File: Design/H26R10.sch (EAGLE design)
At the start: 39 parts, among them P1 HEXABIT_17.32_NO_P3_P6_P7_P12, P2 CON-PHOENIX-350_1751277, P3 1751251, U1 STM32F091CBU6, U2 AD8295BCPZ-WP, U3 AD8275BRMZ, U4 AD7687BRMZ, U5 ADR431ARMZ, X1 XTALL_CSTCE8M00G52

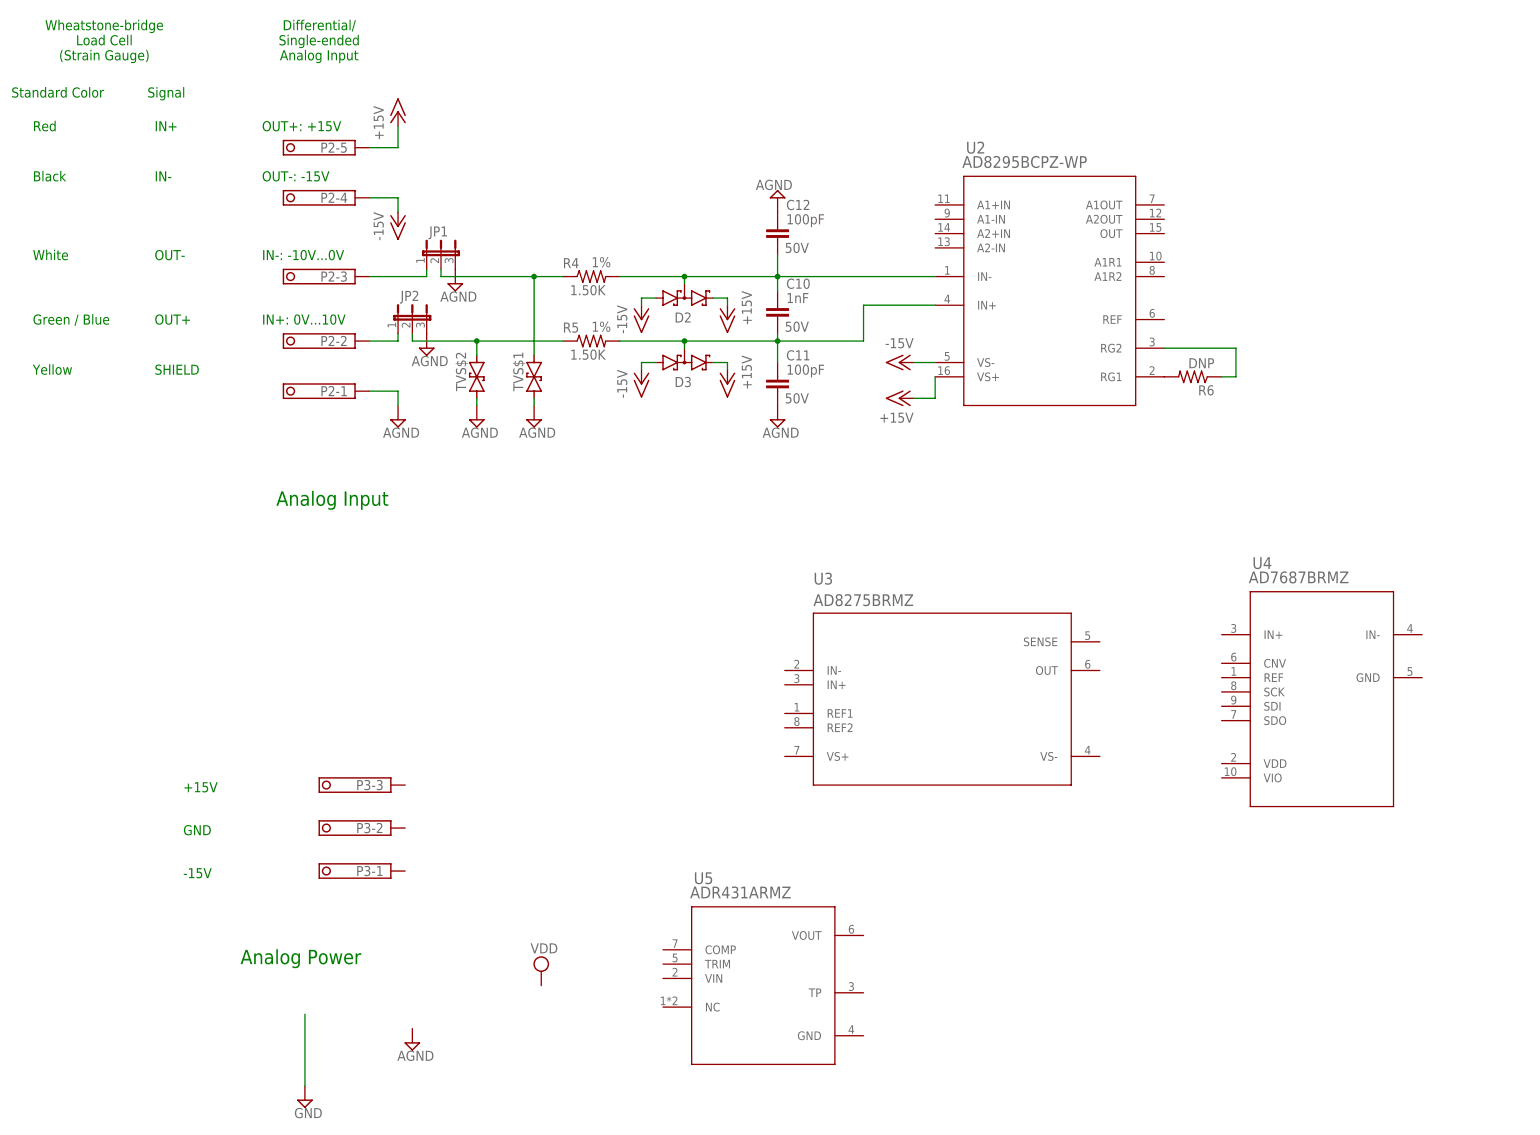
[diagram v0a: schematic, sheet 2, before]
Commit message: Finished analog power chain and some AD8295 connections
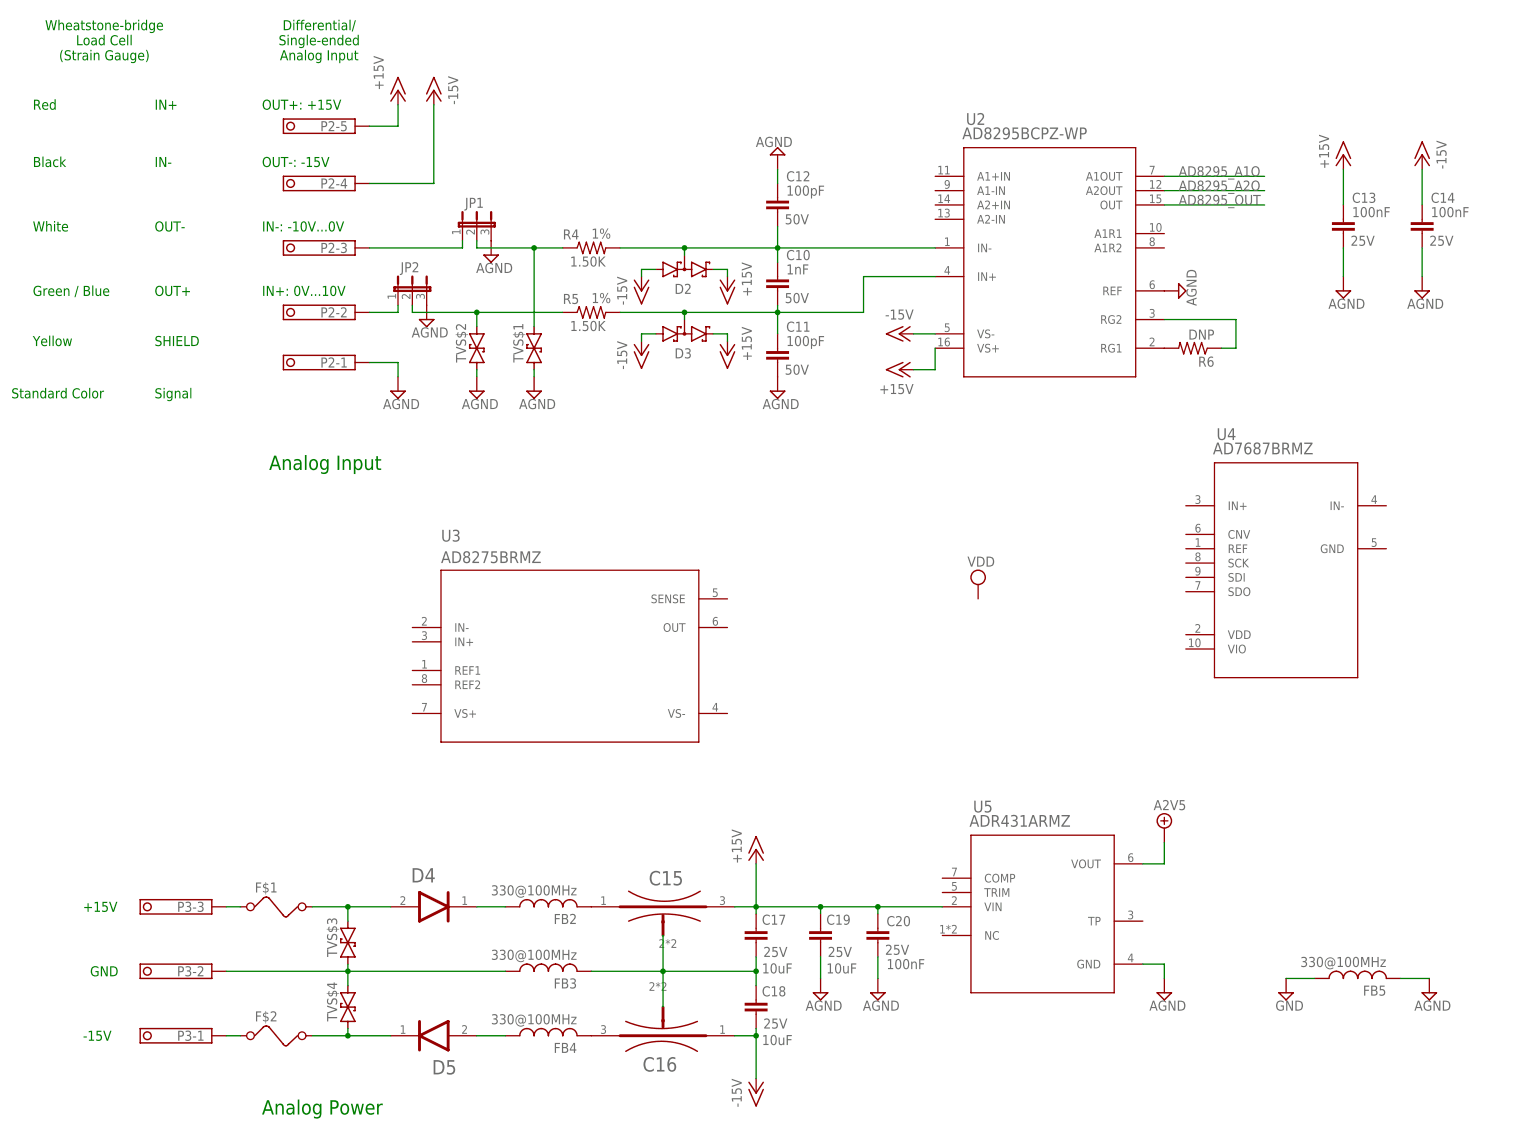
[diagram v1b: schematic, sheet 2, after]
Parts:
- removed FB1: FB-TDK_MMZ1608Y300B, Hexabitz:FB-TDK_MMZ1608Y300B
- added C13, C14, C20: 100nF, Hexabitz:C-0603
- added C15, C16: MURATA_NFM21PC105B1A3DMURATA_NFM21PC105B1A3D_0_0, Hexabitz:MURATA_NFM21PC105B1A3DMURATA_NFM21PC105B1A3D_0_0
- added C17, C18, C19: 10uF, Hexabitz:C-1206
- added D4, D5: DIODES_SBR2U30P1-7DIODES_SBR2U30P1-7_0_0, Hexabitz:DIODES_SBR2U30P1-7DIODES_SBR2U30P1-7_0_0
- added F$1, F$2: NANOSMDC035F-2120, Hexabitz:NANOSMDC035F-2120
- added FB2, FB3, FB4, FB5: 330@100MHz, Hexabitz:FB-0805
- added TVS$3, TVS$4: SMBJ30CA, Hexabitz:SMBJ30CA
- JP1, JP2: MFN (none) -> TE Connectivity; MPN (none) -> 5-146274-3; OCTOPART_URL (none) -> https://octopart.com/5-146274-3-te+connectivity-41331935?r=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
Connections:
- removed net VDDA: C1.1, C2.+, FB1.1, U1.VDDA
- new net +5V: U5.VOUT
- new net AD8295_A1O: U2.A1OUT
- new net AD8295_A2O: U2.A2OUT
- new net AD8295_OUT: U2.OUT
- new net N$15: F$1.1, P3-3.K
- new net N$16: F$2.1, P3-1.K
- new net N$17: D4.ANODE, F$1.2, TVS$3.2
- new net N$18: D5.CATHODE, F$2.2, TVS$4.1
- new net N$19: FB3.1, P3-2.K, TVS$3.1, TVS$4.2
- new net N$20: D4.CATHODE, FB2.1
- new net N$21: D5.ANODE, FB4.1
- new net N$22: C15.INPUT, FB2.2
- new net N$23: C16.OUTPUT, FB4.2
- new net N$24: C17.2, C18.1, FB3.2
- net +15V: now also C13.1, C15.OUTPUT, C17.1, C19.1, C20.1, U5.VIN
- net -15V: now also C14.1, C16.INPUT, C18.2
- net AGND: now also C13.2, C14.2, C19.2, C20.2, FB5.2, U2.REF, U5.GND
- net GND: now also C1.2, C2.-, FB5.1, U1.VSS_A
- net VDD: now also C1.1, C2.+, U1.VDDA; no longer FB1.2
- net VSSA: no longer C1.2, C2.-, U1.VSS_A
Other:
- moved on the sheet: C10, C11, C12, D2, D3, JP1, JP2, P2-1, P2-2, P2-3, P2-4, P2-5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

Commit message: Finished schematics. No ERC yet
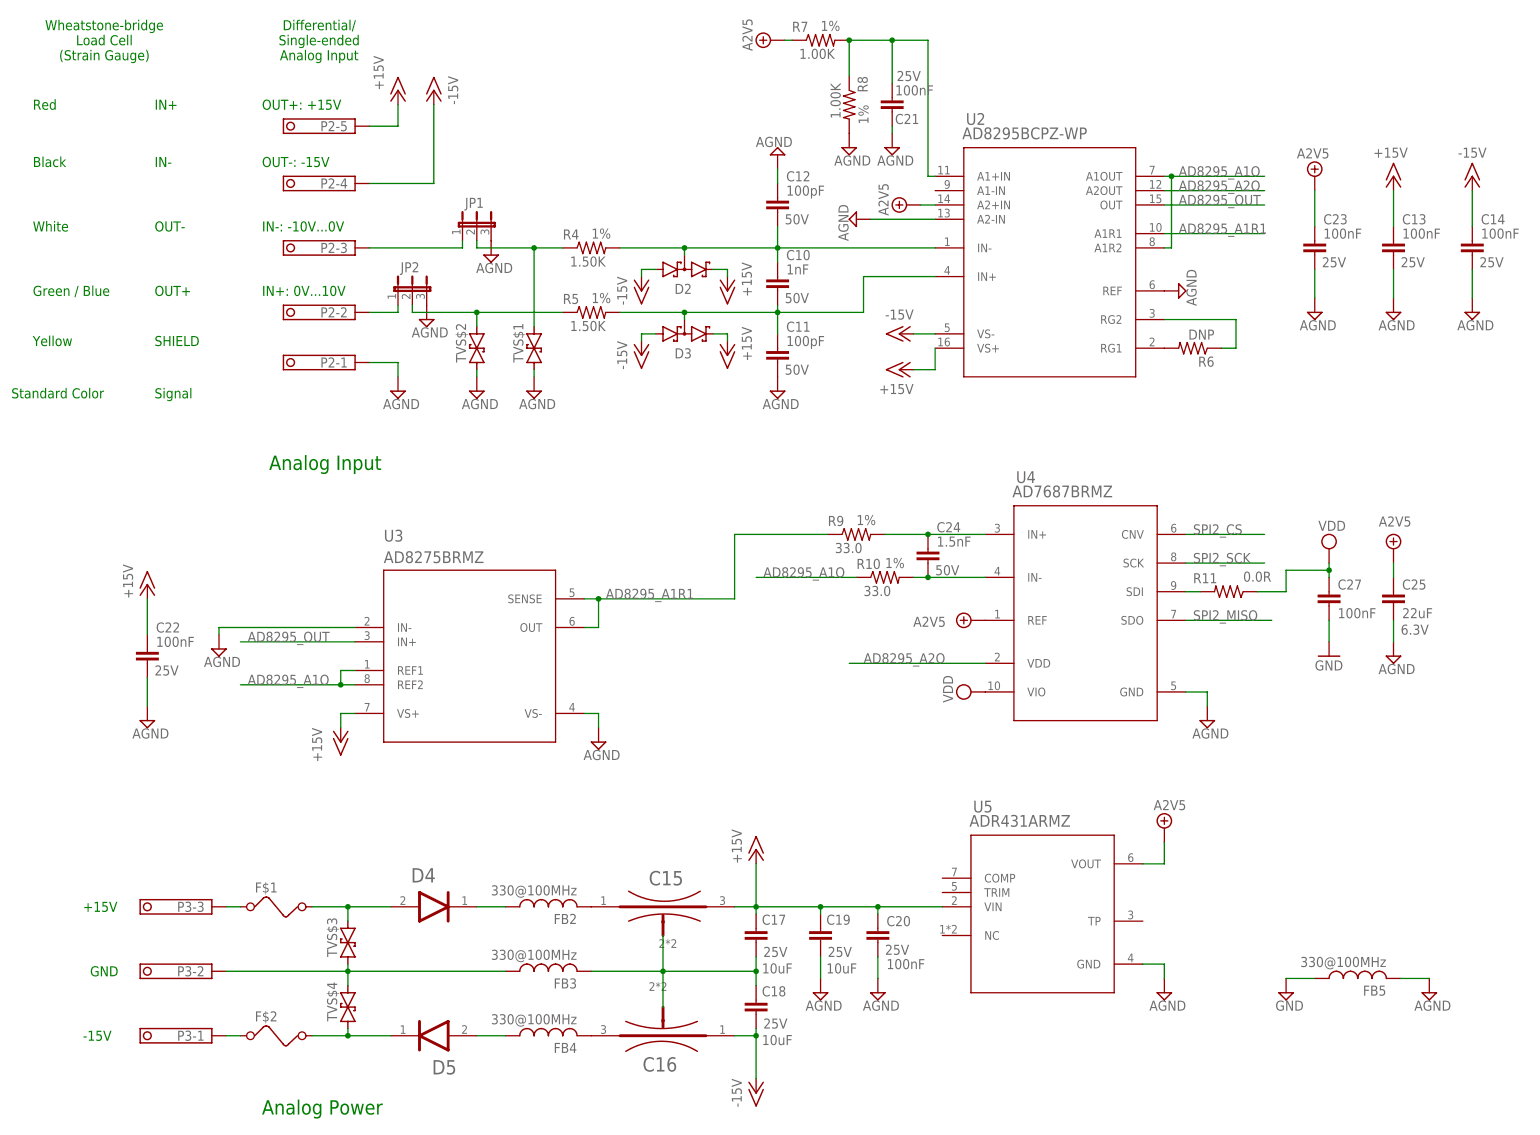
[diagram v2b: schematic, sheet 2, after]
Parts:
- removed R2: 0.0R, Hexabitz:R-0603
- added C21, C22, C23, C27: 100nF, Hexabitz:C-0603
- added C24: 1.5nF, Hexabitz:C-0603
- added C25: 22uF, Hexabitz:C-1206
- added R10, R9: 33.0, Hexabitz:R-0805
- added R11: 0.0R, Hexabitz:R-0603
- added R7, R8: 1.00K, Hexabitz:R-0805
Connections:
- net UART2_RX renamed UART2_RX*
- net UART2_TX renamed UART2_TX*
- removed net VSSA: R2.2
- new net AD8295_A1R1: R9.1, U2.A1R1, U3.OUT, U3.SENSE
- new net N$25: C21.2, R7.2, R8.1, U2.A1+IN
- new net N$26: R11.2, U4.SDI
- new net N$27: C24.1, R9.2, U4.IN+
- new net N$28: C24.2, R10.2, U4.IN-
- new net N$29: P1.SU1
- new net N$30: P1.SU2
- new net N$31: P1.SD1
- new net N$32: P1.SD2
- new net N$33: P1.SU4
- new net N$34: P1.SU5
- new net N$35: P1.SD4
- new net N$36: P1.SD5
- new net SPI2_CS: U1.PB12, U4.CNV
- new net SPI2_MISO: U1.PB14, U4.SDO
- new net SPI2_SCK: U1.PB13, U4.SCK
- net +15V: now also C22.1, U3.VS+
- net +5V: now also C23.1, C25.1, R7.1, U2.A2+IN, U4.REF
- net AD8295_A1O: now also R10.1, U2.A1R2, U3.REF1, U3.REF2
- net AD8295_A2O: now also U4.VDD
- net AD8295_OUT: now also U3.IN+
- net AGND: now also C21.1, C22.2, C23.2, C25.2, R8.2, U2.A2-IN, U3.IN-, U3.VS-, U4.GND
- net GND: now also C27.2; no longer R2.1
- net VDD: now also C27.1, R11.1, U4.VIO
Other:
- note added: "VDD = +3.3V"
- moved on the sheet: C13, C14, U3, U4

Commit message: Renumber schematics Arrange analong path in PCB to estimate footprint Replace module connector with double hexagon Need to replace MCU with bigger package to use 8 UARTs
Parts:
- removed C22: 100nF, Hexabitz:C-0603
- removed FB5: 330@100MHz, Hexabitz:FB-0805
- removed R11: 0.0R, Hexabitz:R-0603
- added C26: 100nF, Hexabitz:C-0603
- added FB1: 330@100MHz, Hexabitz:FB-0805
- added R2: 10.0K, Hexabitz:R-0603
- C10: value 1nF -> 100nF; CAPACITANCE 1nF -> 100nF; MFN KEMET -> Murata; MPN C0603C102J5RACTU -> GRM188R71E104KA01D; OCTOPART_URL https://octopart.com/c0603c102j5ractu-kemet-96704?r=sp&s=FT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 -> https://octopart.com/grm188r71e104ka01d-murata-196239?r=sp&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; TOLERANCE 5% -> 10%; VOLTAGE_RATING 50V -> 25V
- C11, C12: value 100pF -> MURATA_NFM21PC105B1A3DMURATA_NFM21PC105B1A3D_0_0; device Hexabitz:C-0603 -> Hexabitz:MURATA_NFM21PC105B1A3DMURATA_NFM21PC105B1A3D_0_0; CAPACITANCE 100pF -> (none); MFN Vishay -> (none); MPN VJ0603A101JXACW1BC -> (none); OCTOPART_URL https://octopart.com/vj0603a101jxacw1bc-vishay-39475624?r=s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 -> (none); TOLERANCE 5% -> (none); VOLTAGE_RATING 50V -> (none)
- C13, C14: value 100nF -> 10uF; device Hexabitz:C-0603 -> Hexabitz:C-1206; CAPACITANCE 100nF -> (none); MFN Murata -> Yageo; MPN GRM188R71E104KA01D -> CC1206ZKY5V8BB106; OCTOPART_URL https://octopart.com/grm188r71e104ka01d-murata-196239?r=sp&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 -> https://octopart.com/cc1206zky5v8bb106-yageo-42624311?r=sp&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; TOLERANCE 10% -> (none); VOLTAGE (none) -> 25V; VOLTAGE_RATING 25V -> (none)
- C15: value MURATA_NFM21PC105B1A3DMURATA_NFM21PC105B1A3D_0_0 -> 100pF; device Hexabitz:MURATA_NFM21PC105B1A3DMURATA_NFM21PC105B1A3D_0_0 -> Hexabitz:C-0603; CAPACITANCE (none) -> 100pF; MFN (none) -> Vishay; MPN (none) -> VJ0603A101JXACW1BC; OCTOPART_URL (none) -> https://octopart.com/vj0603a101jxacw1bc-vishay-39475624?r=s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; TOLERANCE (none) -> 5%; VOLTAGE_RATING (none) -> 50V
- C16: value MURATA_NFM21PC105B1A3DMURATA_NFM21PC105B1A3D_0_0 -> 1nF; device Hexabitz:MURATA_NFM21PC105B1A3DMURATA_NFM21PC105B1A3D_0_0 -> Hexabitz:C-0603; CAPACITANCE (none) -> 1nF; MFN (none) -> KEMET; MPN (none) -> C0603C102J5RACTU; OCTOPART_URL (none) -> https://octopart.com/c0603c102j5ractu-kemet-96704?r=sp&s=FT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; TOLERANCE (none) -> 5%; VOLTAGE_RATING (none) -> 50V
- C17: value 10uF -> 100pF; device Hexabitz:C-1206 -> Hexabitz:C-0603; CAPACITANCE (none) -> 100pF; MFN Yageo -> Vishay; MPN CC1206ZKY5V8BB106 -> VJ0603A101JXACW1BC; OCTOPART_URL https://octopart.com/cc1206zky5v8bb106-yageo-42624311?r=sp&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 -> https://octopart.com/vj0603a101jxacw1bc-vishay-39475624?r=s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; TOLERANCE (none) -> 5%; VOLTAGE 25V -> (none); VOLTAGE_RATING (none) -> 50V
- C19: value 10uF -> 100nF; device Hexabitz:C-1206 -> Hexabitz:C-0603; CAPACITANCE (none) -> 100nF; MFN Yageo -> Murata; MPN CC1206ZKY5V8BB106 -> GRM188R71E104KA01D; OCTOPART_URL https://octopart.com/cc1206zky5v8bb106-yageo-42624311?r=sp&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 -> https://octopart.com/grm188r71e104ka01d-murata-196239?r=sp&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; TOLERANCE (none) -> 10%; VOLTAGE 25V -> (none); VOLTAGE_RATING (none) -> 25V
- C21: value 100nF -> 1.5nF; CAPACITANCE 100nF -> 1.5nF; MPN GRM188R71E104KA01D -> GRM188R71H152KA01D; OCTOPART_URL https://octopart.com/grm188r71e104ka01d-murata-196239?r=sp&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 -> https://octopart.com/grm188r71h152ka01d-murata-196214?r=sp&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; VOLTAGE_RATING 25V -> 50V
- C23: MFN Murata -> KEMET; MPN GRM188R71E104KA01D -> C0603C104K8RACTU; OCTOPART_URL https://octopart.com/grm188r71e104ka01d-murata-196239?r=sp&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 -> https://octopart.com/c0603c104k8ractu-kemet-145075?r=sp&s=9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; VOLTAGE_RATING 25V -> 10V
- C24: value 1.5nF -> 100nF; CAPACITANCE 1.5nF -> 100nF; MPN GRM188R71H152KA01D -> GRM188R71E104KA01D; OCTOPART_URL https://octopart.com/grm188r71h152ka01d-murata-196214?r=sp&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 -> https://octopart.com/grm188r71e104ka01d-murata-196239?r=sp&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; VOLTAGE_RATING 50V -> 25V
- C27: MFN KEMET -> Murata; MPN C0603C104K8RACTU -> GRM188R71E104KA01D; OCTOPART_URL https://octopart.com/c0603c104k8ractu-kemet-145075?r=sp&s=9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 -> https://octopart.com/grm188r71e104ka01d-murata-196239?r=sp&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; VOLTAGE_RATING 10V -> 25V
- D2, D3: value BAT54S -> DIODES_SBR2U30P1-7DIODES_SBR2U30P1-7_0_0; device Hexabitz:BAT54S -> Hexabitz:DIODES_SBR2U30P1-7DIODES_SBR2U30P1-7_0_0
- D4, D5: value DIODES_SBR2U30P1-7DIODES_SBR2U30P1-7_0_0 -> BAT54S; device Hexabitz:DIODES_SBR2U30P1-7DIODES_SBR2U30P1-7_0_0 -> Hexabitz:BAT54S
- P1: value HEXABIT_17.32_NO_P3_P6_P7_P12 -> HEXABIT_17.32_X2_NO_P5_P10_P11_P20; device hexabitz_connectors:HEXABIT_17.32_NO_P3_P6_P7_P12 -> hexabitz_connectors:HEXABIT_17.32_X2_NO_P5_P10_P11_P20
- R10: value 33.0 -> 0.0R; device Hexabitz:R-0805 -> Hexabitz:R-0603; MFN Vishay -> Yageo; MPN CRCW060333R0FKEA -> RC0603JR-070RL; OCTOPART_URL https://octopart.com/crcw060333r0fkea-vishay-39800560?r=sp&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 -> https://octopart.com/rc0603jr-070rl-yageo-1241539?r=sp&s=X2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; RESISTANCE 33.0 -> 0.0 Ohm; TOLERANCE 1% -> (none)
- R3: value 10.0K -> 1.50K; device Hexabitz:R-0603 -> Hexabitz:R-0805; MFN Yageo -> Vishay; MPN RC0603JR-0710KL -> CRCW08051K50FKEA; OCTOPART_URL https://octopart.com/search?q=RC0603JR-0710KL&start=0 -> https://octopart.com/crcw08051k50fkea-vishay-39438952?r=sp&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; RESISTANCE 10.0K Ohm -> 1.50K; TOLERANCE 5% -> 1%
- R5: value 1.50K -> 1.00K; MFN Vishay -> Yageo; MPN CRCW08051K50FKEA -> RC0603FR-0710KL; OCTOPART_URL https://octopart.com/crcw08051k50fkea-vishay-39438952?r=sp&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 -> https://octopart.com/rc0603fr-0710kl-yageo-40025538?r=sp&s=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; RESISTANCE 1.50K -> 1.00K
- R6: value DNP -> 1.00K; MFN (none) -> Yageo; MPN (none) -> RC0603FR-0710KL; OCTOPART_URL (none) -> https://octopart.com/rc0603fr-0710kl-yageo-40025538?r=sp&s=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; RESISTANCE (none) -> 1.00K; TOLERANCE (none) -> 1%
- R7, R8: value 1.00K -> 33.0; MFN Yageo -> Vishay; MPN RC0603FR-0710KL -> CRCW060333R0FKEA; OCTOPART_URL https://octopart.com/rc0603fr-0710kl-yageo-40025538?r=sp&s=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 -> https://octopart.com/crcw060333r0fkea-vishay-39800560?r=sp&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; RESISTANCE 1.00K -> 33.0
- R9: value 33.0 -> DNP; MFN Vishay -> (none); MPN CRCW060333R0FKEA -> (none); OCTOPART_URL https://octopart.com/crcw060333r0fkea-vishay-39800560?r=sp&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 -> (none); RESISTANCE 33.0 -> (none); TOLERANCE 1% -> (none)
- U2: value AD8295BCPZ-WP -> AD8275BRMZ; device Hexabitz:AD8295BCPZ-WP -> Hexabitz:AD8275BRMZ
- U3: value AD8275BRMZ -> ADR431ARMZ; device Hexabitz:AD8275BRMZ -> Hexabitz:ADR431ARMZ
- U4: value AD7687BRMZ -> AD8295BCPZ-WP; device Hexabitz:AD7687BRMZ -> Hexabitz:AD8295BCPZ-WP
- U5: value ADR431ARMZ -> AD7687BRMZ; device Hexabitz:ADR431ARMZ -> Hexabitz:AD7687BRMZ
- renumbered F$1 to F1, F$2 to F2, P2 to X3, P3 to X2, TVS$1 to TVS4, TVS$2 to TVS3, TVS$3 to TVS1, TVS$4 to TVS2
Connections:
- removed net N$31: P1.SD1
- removed net N$32: P1.SD2
- removed net N$33: P1.SU4
- removed net N$35: P1.SD4
- removed net N$36: P1.SD5
- net +15V: now also C10.1, C11.OUTPUT, C18.1, C24.1, D4.C2, D5.C2, U3.VIN, U4.VS+; no longer C15.OUTPUT, C17.1, C20.1, C22.1, D2.C2, D3.C2, U3.VS+, U5.VIN
- net +5V: now also R5.1, U3.VOUT, U4.A2+IN, U5.REF; no longer C23.1, R7.1, U2.A2+IN, U4.REF, U5.VOUT
- net -15V: now also C12.INPUT, C14.2, C26.1, D4.A1, D5.A1, U4.VS-; no longer C14.1, C16.INPUT, C18.2, D2.A1, D3.A1, U2.VS-
- net AD8295_A1O: now also R8.1, U2.REF1, U2.REF2, U4.A1OUT, U4.A1R2; no longer R10.1, U2.A1OUT, U2.A1R2, U3.REF1, U3.REF2
- net AD8295_A1R1: now also R7.1, U2.OUT, U2.SENSE, U4.A1R1; no longer R9.1, U2.A1R1, U3.OUT, U3.SENSE
- net AD8295_A2O: now also C27.1, U4.A2OUT, U5.VDD; no longer U2.A2OUT, U4.VDD
- net AD8295_OUT: now also U2.IN+, U4.OUT; no longer U2.OUT, U3.IN+
- net AGND: now also C10.2, C15.1, C17.2, C18.2, C20.1, C24.2, C26.2, C27.2, FB4.2, R6.2, U2.IN-, U2.VS-, U3.GND, U4.A2-IN, U4.REF; no longer C11.2, C12.1, C13.2, C14.2, C20.2, C21.1, C22.2, C23.2, FB5.2, R8.2, U2.A2-IN, U2.REF, U3.IN-, U3.VS-, U4.GND
- net B1: now also R2.2; no longer R3.2
- net GND: now also C23.2, FB4.1, P1.GND6, P1.GND7, P1.GND8, P1.GND9, R2.1; no longer C27.2, FB5.1, R3.1
- net N$1: now also JP2.1; no longer JP1.1
- net N$10: now also JP1.2, R4.1; no longer JP2.2, R5.1
- net N$11: now also C15.2, C16.1, D4.C1A2, R3.2, U4.IN-; no longer C10.1, C12.2, D2.C1A2, R4.2, U2.IN-
- net N$12: now also C16.2, C17.1, D5.C1A2, R4.2, U4.IN+; no longer C10.2, C11.1, D3.C1A2, R5.2, U2.IN+
- net N$13: now also R9.2, U4.RG1; no longer R6.2, U2.RG1
- net N$14: now also R9.1, U4.RG2; no longer R6.1, U2.RG2
- net N$17: now also D2.ANODE; no longer D4.ANODE
- net N$18: now also D3.CATHODE; no longer D5.CATHODE
- net N$19: now also FB2.1; no longer FB3.1
- net N$2: now also JP1.1; no longer JP2.1
- net N$20: now also D2.CATHODE, FB1.1; no longer D4.CATHODE, FB2.1
- net N$21: now also D3.ANODE, FB3.1; no longer D5.ANODE, FB4.1
- net N$22: now also C11.INPUT, FB1.2; no longer C15.INPUT, FB2.2
- net N$23: now also C12.OUTPUT, FB3.2; no longer C16.OUTPUT, FB4.2
- net N$24: now also C13.2, C14.1, FB2.2; no longer C17.2, C18.1, FB3.2
- net N$25: now also C20.2, R5.2, R6.1, U4.A1+IN; no longer C21.2, R7.2, R8.1, U2.A1+IN
- net N$26: now also R10.2, U5.SDI; no longer R11.2, U4.SDI
- net N$27: now also C21.1, R7.2, U5.IN+; no longer C24.1, R9.2, U4.IN+
- net N$28: now also C21.2, R8.2, U5.IN-; no longer C24.2, R10.2, U4.IN-
- net N$34: now also P1.SD1, P1.SD2, P1.SD3, P1.SD4, P1.SD6, P1.SD7, P1.SD8, P1.SD9, P1.SU3, P1.SU4, P1.SU6, P1.SU7, P1.SU8, P1.SU9; no longer P1.SU5
- net N$8: now also JP2.2, R3.1; no longer JP1.2, R4.1
- net SPI2_CS: now also U5.CNV; no longer U4.CNV
- net SPI2_MISO: now also U5.SDO; no longer U4.SDO
- net SPI2_SCK: now also U5.SCK; no longer U4.SCK
- net VDD: now also C23.1, P1.VDD6, P1.VDD7, P1.VDD8, P1.VDD9, R10.1, U5.VIO; no longer C27.1, R11.1, U4.VIO
